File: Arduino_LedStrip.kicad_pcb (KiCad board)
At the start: 2 copper layers, 52 x 71 mm, 26 parts, among them J1 Conn_L, J2 Conn_R, J3 LED0, J4 LED1, J5 LED_WS2812B, J6 Barrel_Jack, Q1 IRFZ44N, Q2 IRFZ44N, Q3 IRFZ44N, Q4 IRFZ44N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

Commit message: Routing PCB
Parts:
- added J10: Screw_Terminal_01x01, Mounting_Holes:MountingHole_3.2mm_M3, F.Cu at (150.0, 91.0)
- added J7: Screw_Terminal_01x01, Mounting_Holes:MountingHole_3.2mm_M3, F.Cu at (167.0, 55.5)
- added J8: Screw_Terminal_01x01, Mounting_Holes:MountingHole_3.2mm_M3, F.Cu at (167.5, 92.5)
- added J9: Screw_Terminal_01x01, Mounting_Holes:MountingHole_3.2mm_M3, F.Cu at (125.8, 68.8)
- moved R7 54.6 mm to (136.2, 92.0), turned to 180 degrees
- moved R8 49.5 mm to (136.2, 94.5), turned to 0 degrees
- moved J3 49.2 mm to (154.0, 111.0)
- moved RV1 48.4 mm to (136.0, 81.0), turned to 180 degrees
- moved J4 46.9 mm to (166.5, 111.0)
- moved Q2 41.7 mm to (149.5, 101.0)
- moved R2 41.5 mm to (149.8, 97.1), turned to 0 degrees
- moved U1 40.3 mm to (126.9, 111.0)
- moved SW1 39.9 mm to (125.2, 93.0), turned to 0 degrees
- moved Q3 37.1 mm to (138.5, 101.0)
- moved R3 36.9 mm to (138.8, 97.1), turned to 0 degrees
- moved C1 36.5 mm to (134.5, 72.0)
- moved J6 36.5 mm to (132.5, 64.0)
- moved Q6 35.3 mm to (155.5, 101.0)
- moved R6 35.3 mm to (155.9, 97.1), turned to 0 degrees
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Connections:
- A1 pad 12: /ar_LED0_R -> /ar_LED0_G
- A1 pad 13: /ar_LED0_G -> /ar_LED0_R
- J2 pad 3: /ar_LED0_G -> /ar_LED0_R
- J2 pad 4: /ar_LED0_R -> /ar_LED0_G
- J5 pad 1: +5V -> GND
- J5 pad 3: GND -> +5V
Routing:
- net +12V: track 0.00 -> 166.6 mm
- net GND: track 0.00 -> 150.9 mm, vias 0 -> 1
- net /ar_IR: track 0.00 -> 96.5 mm
- net /ar_Din_LEDWS: track 0.00 -> 58.7 mm, vias 0 -> 2
- net /ar_LED0_B: track 0.00 -> 55.1 mm
- net +5V: track 0.00 -> 50.3 mm
- net /ar_LED0_R: track 0.00 -> 47.9 mm
- net /ar_A2_D16: track 0.00 -> 41.6 mm
- net /ar_LED0_G: track 0.00 -> 40.4 mm
- net /ar_A1_D15: track 0.00 -> 39.9 mm
- net /ar_LED1_B: track 0.00 -> 30.9 mm
- net /ar_LED1_G: track 0.00 -> 28.9 mm
- net /ar_A0_Pot: track 0.00 -> 26.1 mm, vias 0 -> 2
- net /ar_LED1_R: track 0.00 -> 25.9 mm
- net /LED0_B: track 0.00 -> 9.98 mm
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- added copper zone on B.Cu, net GND
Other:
- board size 52 x 71 mm -> 48 x 60.5 mm
- net class Default: clearance 0.2 -> 0.21
- rule trace_clearance: 0.2 -> 0.21

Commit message: Update routing.
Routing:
- net GND: track 150.9 -> 218.2 mm, vias 1 -> 15
- net /ar_Din_LEDWS: track 58.7 -> 59.5 mm
- added copper zone on F.Cu, net GND
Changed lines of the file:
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@@
     (links 83)
     (no_connects 4)
-    (area 122.424999 51.924999 170.575001 112.575001)
+    (area 117.111428 40.3 183.35 121.785001)
     (thickness 1.6)
     (drawings 10)
-    (tracks 233)
+    (tracks 274)
     (zones 0)
     (modules 30)
@@
   )
   (setup
-    (last_trace_width 1)
+    (last_trace_width 0.25)
     (user_trace_width 0.4)
     (user_trace_width 0.75)
@@
     (user_trace_width 3)
     (trace_clearance 0.21)
-    (zone_clearance 0.508)
+    (zone_clearance 0.75)
     (zone_45_only no)
     (trace_min 0.2)
@@
   (segment (start 134.5 82) (end 136 83.5) (width 0.4) (layer F.Cu) (net 6))
   (segment (start 143.5 64.06) (end 139.5 64.06) (width 0.75) (layer F.Cu) (net 6))
+  (segment (start 127.8 61) (end 132.25 61) (width 0.25) (layer F.Cu) (net 7))
+  (segment (start 132.25 61) (end 132.5 60.75) (width 0.25) (layer F.Cu) (net 7))
+  (via (at 132.5 60.75) (size 0.6) (drill 0.4) (layers F.Cu B.Cu) (net 7))
+  (segment (start 124.75 61) (end 124.75 64) (width 0.25) (layer F.Cu) (net 7))
+  (via (at 124.75 64) (size 0.6) (drill 0.4) (layers F.Cu B.Cu) (net 7))
+  (segment (start 132.5 58) (end 129.25 58) (width 0.25) (layer F.Cu) (net 7))
+  (segment (start 129.25 58) (end 128.75 57.5) (width 0.25) (layer F.Cu) (net 7))
+  (via (at 128.75 57.5) (size 0.6) (drill 0.4) (layers F.Cu B.Cu) (net 7))
+  (segment (start 132.5 58) (end 132.5 55) (width 0.25) (layer B.Cu) (net 7))
+  (via (at 132.5 55) (size 0.6) (drill 0.4) (layers F.Cu B.Cu) (net 7))
+  (segment (start 127.8 61) (end 124.75 61) (width 0.25) (layer F.Cu) (net 7))
+  (via (at 124.75 61) (size 0.6) (drill 0.4) (layers F.Cu B.Cu) (net 7))
+  (segment (start 127.8 61) (end 127.8 65.55) (width 2.5) (layer F.Cu) (net 7))
+  (segment (start 149 85) (end 158.12 85) (width 1) (layer B.Cu) (net 7))
+  (segment (start 147.96 85) (end 149 85) (width 1) (layer B.Cu) (net 7))
+  (segment (start 149 85) (end 149 69.5) (width 0.25) (layer B.Cu) (net 7))
+  (segment (start 149 69.5) (end 151.25 67.25) (width 0.25) (layer B.Cu) (net 7))
+  (via (at 151.25 67.25) (size 0.6) (drill 0.4) (layers F.Cu B.Cu) (net 7))
+  (segment (start 167.5 73.5) (end 167.5 63.5) (width 0.25) (layer B.Cu) (net 7))
+  (via (at 167.5 63.5) (size 0.6) (drill 0.4) (layers F.Cu B.Cu) (net 7))
+  (segment (start 167.5 83.5) (end 167.5 73.5) (width 0.25) (layer F.Cu) (net 7))
+  (via (at 167.5 73.5) (size 0.6) (drill 0.4) (layers F.Cu B.Cu) (net 7))
+  (segment (start 162.5 84.38) (end 166.62 84.38) (width 0.25) (layer B.Cu) (net 7))
+  (via (at 167.5 83.5) (size 0.6) (drill 0.4) (layers F.Cu B.Cu) (net 7))
+  (segment (start 166.62 84.38) (end 167.5 83.5) (width 0.25) (layer B.Cu) (net 7))
+  (segment (start 163.5 103.54) (end 166.5 103.54) (width 2) (layer B.Cu) (net 7))
+  (segment (start 161 103.54) (end 163.5 103.54) (width 2) (layer B.Cu) (net 7))
+  (segment (start 163.5 103.54) (end 163.5 102.5) (width 0.25) (layer B.Cu) (net 7))
+  (via (at 163.5 102.5) (size 0.6) (drill 0.4) (layers F.Cu B.Cu) (net 7))
+  (segment (start 158 103.54) (end 161 103.54) (width 2) (layer B.Cu) (net 7))
+  (segment (start 155.5 103.54) (end 158 103.54) (width 2) (layer B.Cu) (net 7))
+  (via (at 158 102.5) (size 0.6) (drill 0.4) (layers F.Cu B.Cu) (net 7))
+  (segment (start 158 103.54) (end 158 102.5) (width 0.25) (layer B.Cu) (net 7))
+  (segment (start 152.75 103.54) (end 152.25 103.04) (width 0.25) (layer B.Cu) (net 7))
+  (segment (start 152.25 103.04) (end 152.25 102.5) (width 0.25) (layer B.Cu) (net 7))
+  (via (at 152.25 102.5) (size 0.6) (drill 0.4) (layers F.Cu B.Cu) (net 7))
+  (segment (start 146.75 103.54) (end 146.75 102.5) (width 0.25) (layer B.Cu) (net 7))
+  (via (at 146.75 102.5) (size 0.6) (drill 0.4) (layers F.Cu B.Cu) (net 7))
+  (segment (start 152.75 103.54) (end 155.5 103.54) (width 2) (layer B.Cu) (net 7))
+  (segment (start 149.5 103.54) (end 152.75 103.54) (width 2) (layer B.Cu) (net 7))
+  (segment (start 146.75 103.54) (end 149.5 103.54) (width 2) (layer B.Cu) (net 7))
+  (segment (start 144 103.54) (end 146.75 103.54) (width 2) (layer B.Cu) (net 7))
+  (segment (start 141.25 103.54) (end 144 103.54) (width 2) (layer B.Cu) (net 7))
+  (segment (start 141.25 103.54) (end 141.25 102.5) (width 0.25) (layer B.Cu) (net 7))
+  (segment (start 138.5 103.54) (end 141.25 103.54) (width 2) (layer B.Cu) (net 7))
+  (via (at 141.25 102.5) (size 0.6) (drill 0.4) (layers F.Cu B.Cu) (net 7))
   (segment (start 139.292857 108.074055) (end 137.324055 108.074055) (width 1) (layer B.Cu) (net 7))
   (segment (start 137.324055 108.074055) (end 136.75 107.5) (width 1) (layer B.Cu) (net 7))
@@
   (segment (start 136.54 103.54) (end 138.5 103.54) (width 1) (layer B.Cu) (net 7))
   (segment (start 143.5 89.46) (end 147.96 85) (width 1) (layer B.Cu) (net 7))
-  (segment (start 147.96 85) (end 158.12 85) (width 1) (layer B.Cu) (net 7))
   (segment (start 158.12 85) (end 158.74 84.38) (width 1) (layer B.Cu) (net 7))
   (segment (start 136 81) (end 136 76.755198) (width 1) (layer B.Cu) (net 7))
@@
   (segment (start 131.244802 72) (end 131 72) (width 1) (layer B.Cu) (net 7))
   (segment (start 138.5 103.54) (end 134 103.54) (width 2) (layer B.Cu) (net 7))
-  (segment (start 161 103.54) (end 166.5 103.54) (width 2) (layer B.Cu) (net 7))
-  (segment (start 155.5 103.54) (end 161 103.54) (width 2) (layer B.Cu) (net 7))
-  (segment (start 149.5 103.54) (end 155.5 103.54) (width 2) (layer B.Cu) (net 7))
-  (segment (start 144 103.54) (end 149.5 103.54) (width 2) (layer B.Cu) (net 7))
-  (segment (start 138.5 103.54) (end 144 103.54) (width 2) (layer B.Cu) (net 7))
   (segment (start 136.75 107.5) (end 136.75 105.29) (width 0.4) (layer B.Cu) (net 7))
   (segment (start 136.75 105.29) (end 138.5 103.54) (width 0.4) (layer B.Cu) (net 7))
   (segment (start 129.46 111) (end 129.5 110.96) (width 0.4) (layer B.Cu) (net 7))
-  (segment (start 127.8 61) (end 127.8 65.55) (width 2.5) (layer F.Cu) (net 7))
   (segment (start 127.8 65.55) (end 129.25 67) (width 2.5) (layer F.Cu) (net 7))
   (segment (start 129.25 67) (end 129.25 70.25) (width 2.5) (layer F.Cu) (net 7))
@@
   (segment (start 139.54 111) (end 139.5 111) (width 0.4) (layer B.Cu) (net 13))
   (segment (start 139.5 111) (end 139.5 110.75) (width 0.4) (layer B.Cu) (net 13))
-  (segment (start 137.75 109) (end 135.75 109) (width 0.4) (layer B.Cu) (net 13))
   (segment (start 139.5 110.75) (end 137.75 109) (width 0.4) (layer B.Cu) (net 13))
-  (segment (start 135.75 109) (end 134.75 108) (width 0.4) (layer B.Cu) (net 13))
-  (segment (start 134.75 108) (end 134.75 106.5) (width 0.4) (layer B.Cu) (net 13))
+  (segment (start 137.75 109) (end 136 109) (width 0.4) (layer B.Cu) (net 13))
+  (segment (start 136 109) (end 134.75 107.75) (width 0.4) (layer B.Cu) (net 13))
+  (segment (start 134.75 107.75) (end 134.75 106.5) (width 0.4) (layer B.Cu) (net 13))
+  (segment (start 151 76.75) (end 151 85) (width 0.4) (layer F.Cu) (net 13))
+  (segment (start 151 85) (end 147.25 88.75) (width 0.4) (layer F.Cu) (net 13))
+  (segment (start 147.25 88.75) (end 147.25 91.75) (width 0.4) (layer F.Cu) (net 13))
+  (segment (start 147.25 91.75) (end 145.25 93.75) (width 0.4) (layer F.Cu) (net 13))
+  (segment (start 145.25 93.75) (end 140.75 93.75) (width 0.4) (layer F.Cu) (net 13))
+  (segment (start 138.75 95.75) (end 136.5 95.75) (width 0.4) (layer F.Cu) (net 13))
+  (segment (start 140.75 93.75) (end 138.75 95.75) (width 0.4) (layer F.Cu) (net 13))
+  (segment (start 136.5 95.75) (end 134.75 97.5) (width 0.4) (layer F.Cu) (net 13))
   (segment (start 134.75 97.5) (end 134.75 106.5) (width 0.4) (layer F.Cu) (net 13))
-  (segment (start 136.5 95.75) (end 134.75 97.5) (width 0.4) (layer F.Cu) (net 13))
-  (segment (start 140.75 93.75) (end 138.75 95.75) (width 0.4) (layer F.Cu) (net 13))
-  (segment (start 143.744055 93.75) (end 140.75 93.75) (width 0.4) (layer F.Cu) (net 13))
-  (segment (start 151 86.494055) (end 143.744055 93.75) (width 0.4) (layer F.Cu) (net 13))
-  (segment (start 138.75 95.75) (end 136.5 95.75) (width 0.4) (layer F.Cu) (net 13))
-  (segment (start 151 76.75) (end 151 86.494055) (width 0.4) (layer F.Cu) (net 13))
   (via (at 134.75 106.5) (size 0.6) (drill 0.4) (layers F.Cu B.Cu) (net 13))
   (segment (start 158.74 76.76) (end 151.01 76.76) (width 0.4) (layer B.Cu) (net 13))
@@
       )
     )
+  )
+  (zone (net 7) (net_name GND) (layer F.Cu) (hatch edge 0.508)
+    (connect_pads (clearance 0.75))
+    (min_thickness 0.254)
+    (fill yes (arc_segments 16) (thermal_gap 0.508) (thermal_bridge_width 0.508))
+    (polygon
+      (pts
+        (xy 119 116) (xy 172 116) (xy 172 50) (xy 119 50)
+      )
+    )

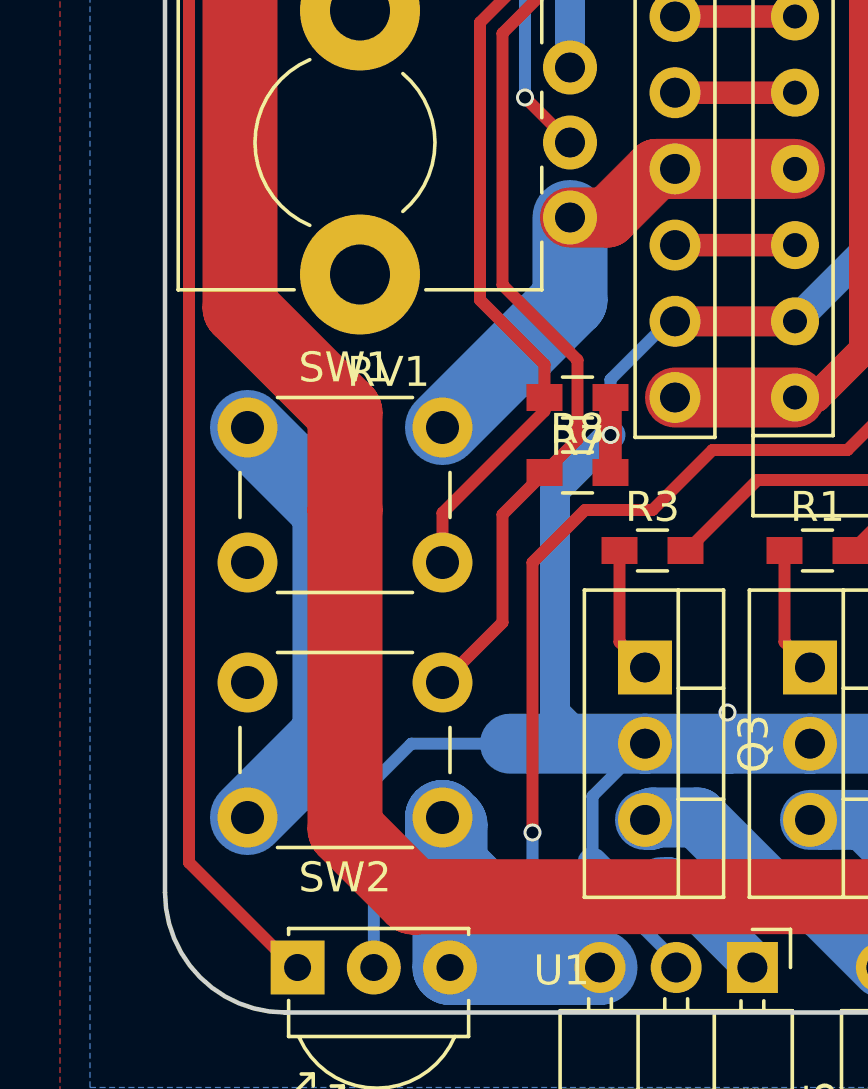
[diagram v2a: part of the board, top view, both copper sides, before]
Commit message: Rotate SW1 and SW2.
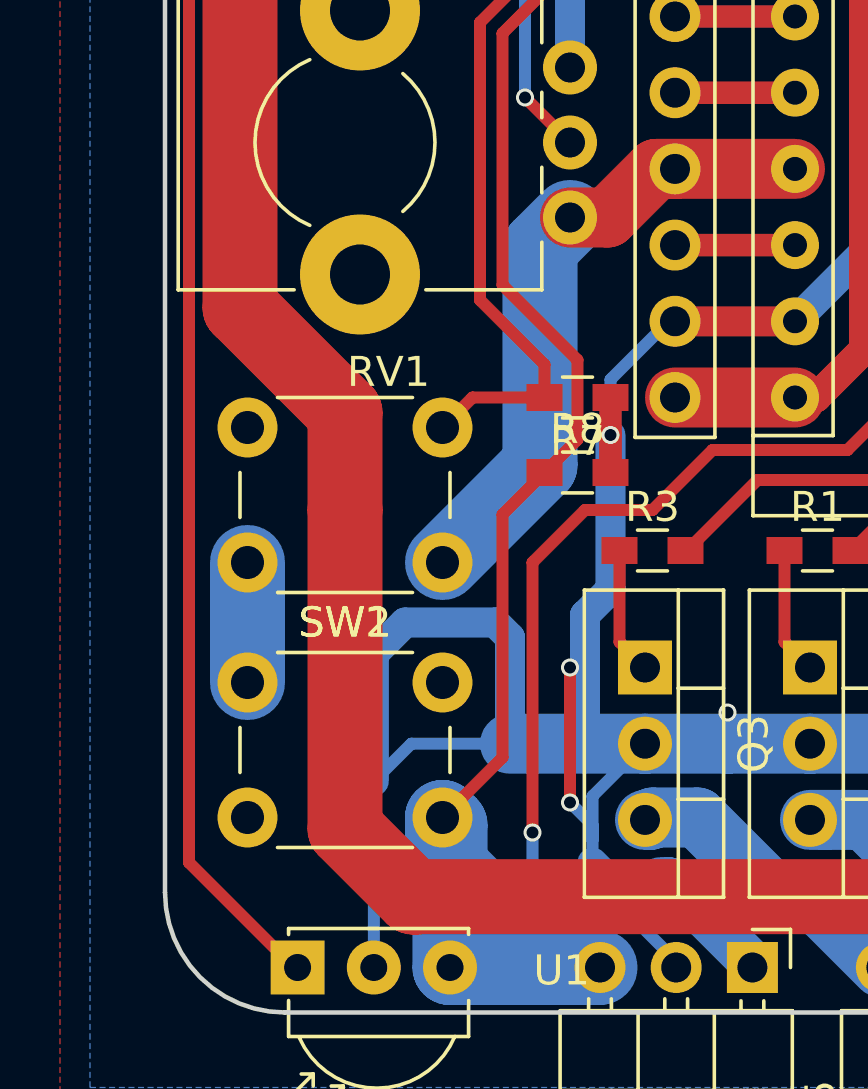
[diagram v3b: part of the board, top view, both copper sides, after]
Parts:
- moved SW1 7.91 mm to (131.8, 97.5), turned to 180 degrees
- moved SW2 7.91 mm to (125.2, 101.5), turned to 0 degrees
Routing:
- net GND: track 218.2 -> 236.4 mm, vias 15 -> 17
- net +5V: track 50.3 -> 43.6 mm
- net /ar_A2_D16: track 41.6 -> 46.1 mm
- net /ar_A1_D15: track 39.9 -> 36.8 mm
